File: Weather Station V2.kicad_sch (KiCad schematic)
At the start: 49 parts, among them J1 SOLAR IN, J2 18650, J3 Battery_AUX, J6 USB_C, J7 RYLR998, J8 Breakout, Q1 AO4842, Q2 DMP2240UDM-7, SW1 LED_ENABLE, SW2 EN/RST, SW3 BOOT, SW4 POWER_SELECT, SW6 POWER, U1 TP4056, U2 DW01A, U3 LDL1117S33R, U5 ESP32-S3-WROOM-1U, U7 USBLC6-2SC6

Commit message: - Chnaged to USBLC6-2SC6 for USB ESD protection - Expose 5V rail to Breakout - Fixed missing battery track to power sensors;
- TO DO: open collector mosfet driver to 5V reg
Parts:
- R3: value 1K -> 3K
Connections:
- net CHRG renamed ~{CHRG}
- net STDBY renamed ~{STDBY}
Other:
- moved on the sheet: C2, Q1A, Q1B, R1, R16, R2, R6, U2

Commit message: - Connected open collector mosfet driver to 5V reg - Re-routed tracks related to NMOS
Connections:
- net ~{SENSOR_EN} renamed SENSOR_EN
- no-connect marks 19 -> 22
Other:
- sheet Sensors Interface ports: added SENSOR_EN; removed ~{SENSOR_EN}
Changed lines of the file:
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@@
 	)
 	(no_connect
+		(at 83.82 80.01)
+	)
+	(no_connect
 		(at 114.3 41.91)
 	)
 	(no_connect
+		(at 83.82 59.69)
+	)
+	(no_connect
 		(at 114.3 49.53)
 	)
@@
 	)
 	(no_connect
+		(at 83.82 74.93)
+	)
+	(no_connect
 		(at 114.3 62.23)
 	)
@@
 		)
 	)
-	(label "~{SENSOR_EN}"
+	(label "SENSOR_EN"
 		(at 99.06 139.7 0)
 		(effects
@@
 		)
 	)
-	(label "~{SENSOR_EN}"
+	(label "SENSOR_EN"
 		(at 80.01 54.61 180)
 		(effects
@@
 			)
 		)
-		(pin "~{SENSOR_EN}" input
+		(pin "SENSOR_EN" input
 			(at 95.25 139.7 0)
 			(effects

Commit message: - Fixed Back to Back mosfet (now the follow DW01A datasheet) - Connected STDBY and CHRG leds to Vin - Removed STDBY and CHRG mcu monitoring (risk of frying the pins) - TP4056 Vcc cap 0.1 to 10 uf - Added BAT+ coupling cap STDBY and CHRG
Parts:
- added C10: 10u, Capacitor_SMD:C_1206_3216Metric, symbol Device:C_Small
- C3: value 0.1u -> 10u
- R4, R5: value 330 -> 1k
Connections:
- net +3V3: no longer SW1.1 (A)
- net BAT+: now also C10.1
- net BAT-: now also Q1.3 (S2); no longer Q1.5 (D2), Q1.6 (D2)
- net GND: now also C10.2
- net Vin: now also SW1.1 (A)
- net at Q1.7 (D1), Q1.8 (D1): now also Q1.5 (D2), Q1.6 (D2); no longer Q1.3 (S2)
- net ~{CHRG}: no longer names the net of R5.2, U1.7 (~{CHRG})
- net ~{CHRG}: no longer U5.25 (IO48)
- net ~{STDBY}: no longer names the net of R4.2, U1.6 (~{STDBY})
- net ~{STDBY}: no longer U5.24 (IO47)
- no-connect marks 22 -> 24
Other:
- moved on the sheet: C3, Q1B

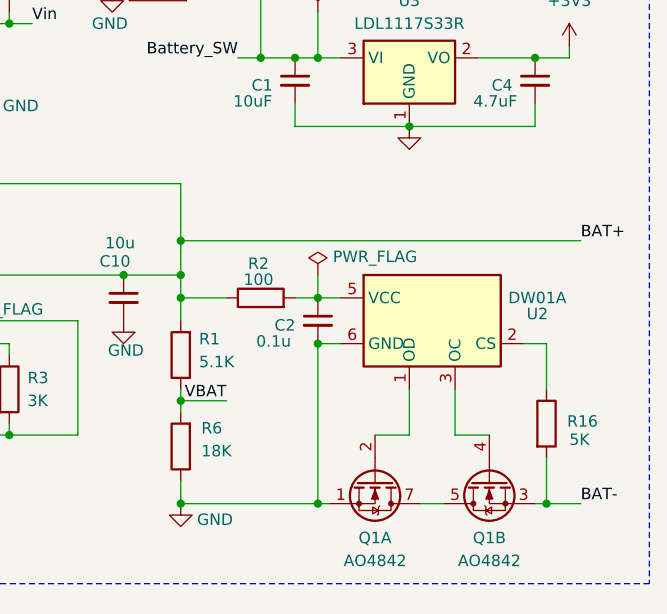
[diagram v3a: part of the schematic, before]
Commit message: - Changed revision to Rev 3 - Removed Production Folder - Changed DW01A Resistor value to match datasheet
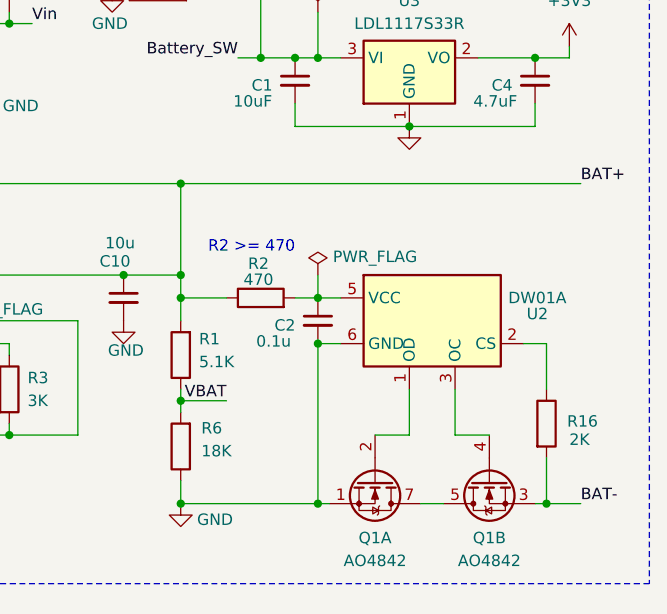
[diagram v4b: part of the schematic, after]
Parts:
- R16: value 5K -> 2K
- R2: value 100 -> 470
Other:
- note added: "R2 >= 470"
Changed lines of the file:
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@@
 		(title "Weather Station V2")
 		(date "2025-12-05")
-		(rev "2.2")
+		(rev "3")
 		(company "Maurizio Gasperoni")
 	)
@@
 		)
 	)
+	(text "R2 >= 470"
+		(exclude_from_sim no)
+		(at 237.744 57.912 0)
+		(effects
+			(font
+				(size 1.27 1.27)
+			)
+		)
+	)
 	(text "PMOS!\n"
 		(exclude_from_sim no)
@@
 	)
 	(junction
-		(at 229.87 57.15)
-		(diameter 0)
-		(color 0 0 0 0)
-	)
-	(junction
 		(at 44.45 40.64)
 		(diameter 0)
@@
 	)
 	(junction
+		(at 229.87 50.8)
+		(diameter 0)
+		(color 0 0 0 0)
+	)
+	(junction
 		(at 173.99 85.09)
 		(diameter 0)
@@
 	(wire
 		(pts
-			(xy 274.32 57.15) (xy 229.87 57.15)
+			(xy 274.32 50.8) (xy 229.87 50.8)
 		)
 		(stroke
@@
 	(wire
 		(pts
+			(xy 229.87 50.8) (xy 229.87 60.96)
+		)
+		(stroke
+			(width 0)
+			(type default)
+		)
+	)
+	(wire
+		(pts
 			(xy 196.85 106.68) (xy 203.2 106.68)
 		)
@@
 	(wire
 		(pts
-			(xy 229.87 50.8) (xy 229.87 57.15)
-		)
-		(stroke
-			(width 0)
-			(type default)
-		)
-	)
-	(wire
-		(pts
 			(xy 247.65 152.4) (xy 257.81 152.4)
 		)
@@
 	(wire
 		(pts
-			(xy 229.87 57.15) (xy 229.87 60.96)
-		)
-		(stroke
-			(width 0)
-			(type default)
-		)
-	)
-	(wire
-		(pts
 			(xy 255.27 44.45) (xy 269.24 44.45)
 		)
@@
 	)
 	(label "BAT+"
-		(at 274.32 57.15 0)
+		(at 274.32 50.8 0)
 		(effects
 			(font
@@
 			)
 		)
-		(property "Value" "100"
+		(property "Value" "470"
 			(at 238.506 61.468 90)
 			(show_name no)
@@
 			)
 		)
-		(property "Value" "5K"
+		(property "Value" "2K"
 			(at 273.05 79.248 0)
 			(show_name no)
